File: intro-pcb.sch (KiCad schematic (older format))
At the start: 24 parts, among them SW1 SW_Push, U1 ATmega32U4-AU, Y1 Crystal_GND24_Small

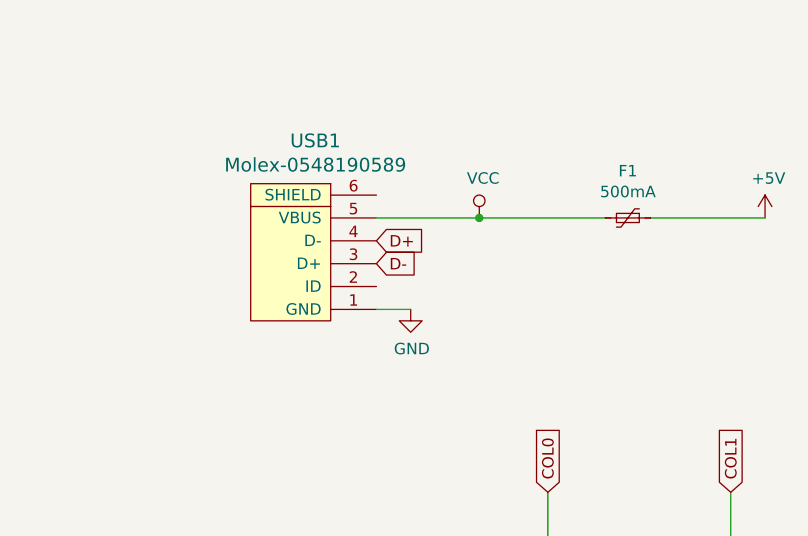
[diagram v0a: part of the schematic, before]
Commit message: Added traces
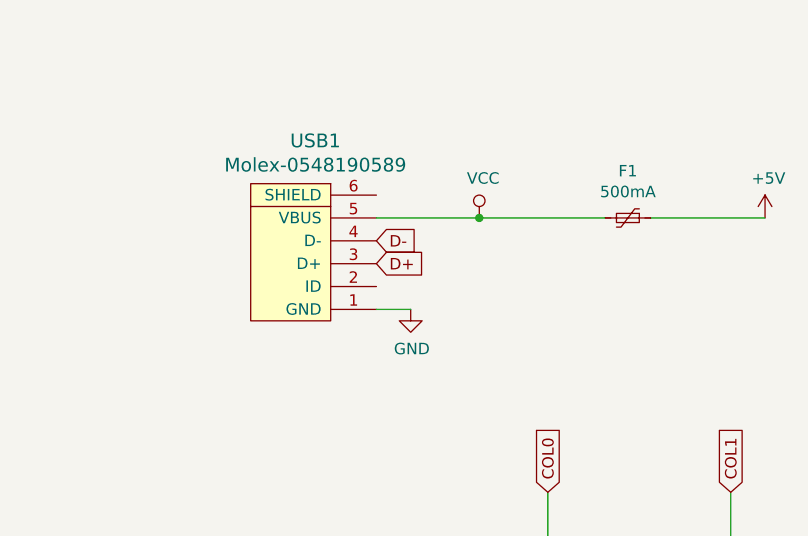
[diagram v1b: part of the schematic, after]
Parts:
- MX1, MX2, MX3, MX4: footprint MX_Only:MXOnly-1U-NoLED -> MX_Alps_Hybrid:MX-1U-NoLED
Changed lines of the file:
@@
 	8050 1900 8600 1900
 Text GLabel 7600 2000 2    50   Input ~ 0
+D-
+Text GLabel 7600 2100 2    50   Input ~ 0
 D+
-Text GLabel 7600 2100 2    50   Input ~ 0
-D-
 $Comp
 L power:GND #PWR0113
@@
 F 0 "MX1" H 8233 3773 60  0000 C CNN
 F 1 "MX-NoLED" H 8233 3699 20  0000 C CNN
-F 2 "MX_Only:MXOnly-1U-NoLED" H 7575 3525 60  0001 C CNN
+F 2 "MX_Alps_Hybrid:MX-1U-NoLED" H 7575 3525 60  0001 C CNN
 F 3 "" H 7575 3525 60  0001 C CNN
 	1    8200 3550
@@
 F 0 "MX3" H 9033 3773 60  0000 C CNN
 F 1 "MX-NoLED" H 9033 3699 20  0000 C CNN
-F 2 "MX_Only:MXOnly-1U-NoLED" H 8375 3525 60  0001 C CNN
+F 2 "MX_Alps_Hybrid:MX-1U-NoLED" H 8375 3525 60  0001 C CNN
 F 3 "" H 8375 3525 60  0001 C CNN
 	1    9000 3550
@@
 F 0 "MX2" H 8233 4573 60  0000 C CNN
 F 1 "MX-NoLED" H 8233 4499 20  0000 C CNN
-F 2 "MX_Only:MXOnly-1U-NoLED" H 7575 4325 60  0001 C CNN
+F 2 "MX_Alps_Hybrid:MX-1U-NoLED" H 7575 4325 60  0001 C CNN
 F 3 "" H 7575 4325 60  0001 C CNN
 	1    8200 4350
@@
 F 0 "MX4" H 9033 4573 60  0000 C CNN
 F 1 "MX-NoLED" H 9033 4499 20  0000 C CNN
-F 2 "MX_Only:MXOnly-1U-NoLED" H 8375 4325 60  0001 C CNN
+F 2 "MX_Alps_Hybrid:MX-1U-NoLED" H 8375 4325 60  0001 C CNN
 F 3 "" H 8375 4325 60  0001 C CNN
 	1    9000 4350
